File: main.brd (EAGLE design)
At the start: 100 x 50 mm, 116 parts, among them IC1 PM8834-SO08N, IC17 LD398533RM, IC18 LD1117S50TR, IC2 PM8834-SO08N, IC4 CP2102, J1 RJ11, Q1 IRF3205SPBF, Q11 BSS138, Q12 BSS138, Q13 BSS138, Q2 IRF3205SPBF, Q3 IRF3205SPBF, Q4 IRF3205SPBF, Q5 BSS138, Q6 BSS138, Q7 BSS138, Q8 BSS138, Q9 BSS138, T1 SS8050-G, T2 SS8050-G, U1 TMP275AIDR, U4 ESP-WROOM-32, X2 1751248, X4 1751277, X5 1751280

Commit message: Layout
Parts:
- removed C28, C29: 12pF, resistor:C0805
- removed C56, C62: 100nF, resistor:C0805
- removed C57: 10nF X7R, resistor:C0805
- removed C58, C61: 1uF_X5R, resistor:C0805
- removed C59, C60: 10uF, resistor:SMC_C
- removed D14: BAT60JFILM, diode:SOD323-W
- removed IC17: LD398533RM, st-microelectronics:SOT23-5L
- removed IC18: LD1117S50TR, v-reg:SOT223
- removed JP6: (no value), adafruit:1X03
- removed LED14: ROOD, led:CHIP-LED0805
- removed LED2: RGBLED5050, adafruit:RGBLED5050
- removed R44, R45: 10K, resistor:R0805
- removed R46: 10R, resistor:R0805
- removed R47: X, resistor:R0805
- removed R48: 1K, resistor:R0805
- removed U4: ESP-WROOM-32, esp32:ESP-WROOM-32
- removed X5: 1751280, con-phoenix-350:1751280
- added C17, C18, C20: 100n, resistor:C0805
- added C19, C7: 100nF, resistor:C0805
- added C21, C22: 1uF X7R, resistor:C0805
- added C9: (no value), resistor:SMC_A
- added IC3: CP2102, silabs:MLP28
- added IC5: PM8834-SO08N, PM8834:SO08N
- added JP2: (no value), adafruit:1X03
- added LED1: RGBLED5050, adafruit:RGBLED5050
- added U2: TMP275AIDR, TMP275AIDR:SOIC127P600X175-8N
- added X1: 1751248, con-phoenix-350:1751248
- C1: value 100n -> 10uF; device resistor:C0805 -> resistor:SMC_C
- C10: value 100n -> 1uF_X5R
- C11: value (none) -> 100nF; device resistor:SMC_A -> resistor:C0805
- C14, C15: value 100n -> 12pF
- C2: value 100nF -> 10uF; device resistor:C0805 -> resistor:SMC_C
- C3: value 100nF -> 1uF_X5R
- C5: value 1uF_X5R -> 10nF X7R
- C6: value 1uF X7R -> 1uF_X5R
- C8: value 1uF X7R -> 100nF
- D1, D2: value BAT54S -> BAT60JFILM; device diode:SOT23 -> diode:SOD323-W
- D5: value BAT60JFILM -> BAT54S; device diode:SOD323-W -> diode:SOT23
- IC1: value PM8834-SO08N -> LD1117S50TR; device PM8834:SO08N -> v-reg:SOT223
- IC2: value PM8834-SO08N -> LD398533RM; device PM8834:SO08N -> st-microelectronics:SOT23-5L
- IC4: value CP2102 -> PM8834-SO08N; device silabs:MLP28 -> PM8834:SO08N
- Q1: value IRF3205SPBF -> (none); device IRF3205SPBF:TRANS_IRF3205SPBF -> crystal:TC38H
- Q10: value (none) -> IRF3205SPBF; device crystal:TC38H -> IRF3205SPBF:TRANS_IRF3205SPBF
- Q11, Q12, Q13: value BSS138 -> IRF3205SPBF; device SparkFun:SOT23-3 -> IRF3205SPBF:TRANS_IRF3205SPBF
- Q2, Q3, Q4: value IRF3205SPBF -> BSS138; device IRF3205SPBF:TRANS_IRF3205SPBF -> SparkFun:SOT23-3
- R1: value 10K -> 22K1
- R10: value 10R -> 10K
- R11, R12, R29: value 10K -> 4K7
- R15, R16: value X -> 10K
- R17, R18, R38, R39: value 1K -> 10K
- R2: value 10R -> 47K5
- R21, R22: value 10K -> X
- R23, R24: value 10K -> 10R
- R25, R26, R34: value 10K -> 1K
- R3, R4: value 4K7 -> 1K
- R31, R32: value 0R -> 10K
- R33: value 2K -> 10K
- R35: value 22K1 -> 10K
- R36: value 47K5 -> 10K
- R5: value 4K7 -> 2K
- R7, R8: value 1K -> 0R
- S1: value (none) -> MOMENTARY-SWITCH-SPST-SMD-5.2-REDUNDANT; device switch-omron:B3F-10XX -> SparkFun-Switches:TACTILE_SWITCH_SMD_5.2MM
- U1: value TMP275AIDR -> ESP-WROOM-32; device TMP275AIDR:SOIC127P600X175-8N -> esp32:ESP-WROOM-32
- X2: value 1751248 -> 1751280; device con-phoenix-350:1751248 -> con-phoenix-350:1751280
- moved Q12 160.0 mm to (30.8, 6.03), turned to 270 degrees
- moved Q11 151.7 mm to (30.8, -6.03), turned to 270 degrees
- moved R40 147.9 mm to (9.84, 12.4), turned to 180 degrees
- moved R6 138.8 mm to (-6.99, -9.21), turned to 180 degrees
- moved C15 129.6 mm to (-19.7, 5.71), turned to 180 degrees
- moved D3 124.1 mm to (-40.3, 7.94), turned to 270 degrees
- moved Q9 104.5 mm to (-20.3, -7.30)
- moved Q4 103.6 mm to (-34.3, -62.5), turned to 90 degrees
- moved X2 94.1 mm to (-46.4, 4.76), turned to 270 degrees
- moved R29 93.1 mm to (9.84, 16.8), turned to 180 degrees
- moved R20 92.0 mm to (-37.1, -66.7), turned to 270 degrees
- moved Q3 91.6 mm to (-34.3, -58.4), turned to 90 degrees
- moved R19 91.2 mm to (-31.4, -66.7), turned to 90 degrees
- moved H1 90.0 mm to (45.0, 20.0)
- moved H2 90.0 mm to (45.0, -20.0)
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- renumbered C30 to C16, CN2 to CN1, S3 to S2, X4 to X3
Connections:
- removed net LED: U4.12
- removed net N$22: X5.1
- removed net N$28: Q13.3, R41.1
- removed net N$30: LED2.5, R40.1
- removed net N$33: D3.3, R46.2, R48.1
- removed net N$37: Q12.1
- removed net N$4: X5.4
- removed net N$40: Q11.1
- removed net N$41: Q9.1
- removed net N$99: LED14.A, R39.1
- new net LEDB: Q8.1, U1.12
- new net LEDG: Q7.1, U1.11
- new net LEDR: Q6.1, U1.10
- new net P1: Q9.3, R35.1, U1.16
- net +12V: now also C1.+, C21.1, C22.1, IC1.3, IC4.6, IC5.6, R38.2, R39.2, R42.2, R43.2, X1.1; no longer C59.+, C6.1, C8.1, IC1.6, IC18.3, IC2.6, R11.2, R12.2, R13.2, R14.2, X2.1
- net +3V3: now also C10.1, C11.1, C19.1, C6.1, C7.1, C8.1, C9.+, D4.2, IC2.5, IC3.6, IC3.7, LED1.1, LED1.2, LED1.3, Q2.1, Q3.1, Q4.1, R11.2, R12.2, R13.1, R15.1, R17.1, R19.1, R27.2, R28.2, R29.2, R35.2, U1.2, U2.8; no longer C11.+, C12.1, C13.1, C4.1, C5.1, C61.1, C62.1, D1.2, D2.2, IC17.5, IC4.6, IC4.7, LED2.1, LED2.2, LED2.3, Q6.1, Q7.1, Q8.1, R1.2, R23.1, R25.1, R27.1, R29.1, R33.2, R41.2, R6.2, R7.2, R8.2, R9.2, U1.8, U4.2
- net +5V: now also C3.1, C4.1, D1.C, D2.C, D5.2, IC2.1, IC2.3, JP1.1, R14.1, R33.2, X2.1, X2.4; no longer C56.1, C58.1, D14.C, D4.2, D5.C, IC17.1, IC17.3, JP6.1, R24.1, R37.2
- net BTN: now also C13.1, R4.1, S1.3, S1.4, U1.6; no longer C2.1, R8.1, S1.1, U4.6
- net CTS: now also IC3.23; no longer IC4.23
- net DCD: now also IC3.1; no longer IC4.1
- net DSR: now also IC3.27; no longer IC4.27
- net DTR: now also IC3.28, R9.1; no longer IC4.28, R42.1
- net EN: now also C12.1, R3.1, U1.3; no longer C3.1, R7.1, U4.3
- net GND: now also C1.-, C11.2, C17.2, C18.2, C19.2, C2.-, C20.2, C21.2, C22.2, C7.2, C9.-, D5.1, IC1.1, IC2.2, IC3.3, IC3.EXP, IC3.M, IC5.3, JP2.3, Q10.3, Q11.3, Q12.3, Q13.3, Q6.2, Q7.2, Q8.2, R2.1, R21.1, R22.1, R36.2, R37.2, R40.2, R41.2, R6.2, S1.1, S1.2, U1.1, U1.15, U1.38, U2.4, U2.5, U2.6, U2.7, X1.2, X2.3, X2.6; no longer C1.2, C11.-, C2.2, C28.2, C29.2, C56.2, C57.2, C58.2, C59.-, C60.-, C61.2, C62.2, D1.1, D2.1, IC1.3, IC17.2, IC18.1, IC2.3, IC4.EXP, IC4.M, JP6.3, LED14.C, Q1.3, Q11.2, Q12.2, Q13.2, Q2.3, Q3.3, Q4.3, R15.1, R16.1, R19.2, R20.2, R21.2, R22.2, R34.2, R36.1, R47.1, S1.3, U1.4, U1.5, U1.6, U1.7, U4.1, U4.15, U4.38, X2.2, X5.3, X5.6
- net HV: now also JP2.1, R16.1, R18.1, R20.1; no longer JP1.1, R26.1, R28.1, R30.1
- net HV1: now also JP1.2, Q2.3, R14.2; no longer JP6.2, Q5.3, R24.2
- net HV2: now also JP2.2, Q3.3, R16.2; no longer JP1.2, Q6.3, R26.2
- net HV3: now also Q4.3, R18.2; no longer Q7.3, R28.2
- net HV4: now also Q5.3, R20.2; no longer Q8.3, R30.2
- net I2C_SCL: now also R12.1, U1.36, U2.2; no longer R4.1, U1.2, U4.36
- net I2C_SDA: now also R11.1, U1.37, U2.1; no longer R3.1, U1.1, U4.37
- net INP1: now also C17.1, R25.2, R27.1, U1.13; no longer C10.1, R17.2, R9.1, U4.11
- net INP2: now also C18.1, R26.2, R28.1, U1.14; no longer C1.1, C15.1, R1.1, R18.2, R48.2, R6.1, U4.10
- net IO0: now also U1.25; no longer U4.25
- net LV0: now also Q2.2, R13.2; no longer Q5.2, R23.2
- net LV1: now also Q3.2, R15.2; no longer Q6.2, R25.2
- net LV2: now also Q4.2, R17.2; no longer Q7.2, R27.2
- net LV3: now also Q5.2, R19.2; no longer Q8.2, R29.2
- net N$1: now also Q6.3, R30.2; no longer Q9.3, R40.2
- net N$10: now also IC4.4, R38.1; no longer IC1.4, R11.1
- net N$102: now also C5.1, IC2.4; no longer C57.1, IC17.4
- net N$11: now also LED1.5, R31.1; no longer LED2.6, R44.1
- net N$12: now also IC4.7, Q11.1; no longer IC1.7, Q2.1
- net N$13: now also IC4.5, Q10.1; no longer IC1.5, Q1.1
- net N$14: now also Q11.2; no longer Q2.2
- net N$15: now also IC5.7, Q13.1; no longer IC2.7, Q4.1
- net N$16: now also IC5.5, Q12.1; no longer IC2.5, Q3.1
- net N$17: now also Q12.2; no longer Q3.2
- net N$18: now also Q13.2; no longer Q4.2
- net N$19: now also IC3.11, R6.1; no longer IC4.11, R34.1
- net N$2: now also R22.2, R24.1, X2.5; no longer R15.2, R2.1, X5.5
- net N$20: now also R21.2, R23.1, X2.2; no longer R10.1, R16.2, X5.2
- net N$2001: now also IC5.4, R43.1; no longer IC2.4, R14.1
- net N$21: now also IC3.9, R5.1; no longer IC4.9, R33.1
- net N$23: now also C2.+, D1.A, IC1.4; no longer C60.+, D14.A, IC18.4, R39.2
- net N$24: now also IC3.8, R1.2, R2.2; no longer IC4.8, R35.2, R36.2
- net N$25: now also IC3.5; no longer IC4.5
- net N$26: now also R33.1, R34.1; no longer R37.1, R38.1
- net N$27: now also C20.1, D5.3, Q9.1, R34.2; no longer C14.1, D4.3, Q13.1, R38.2
- net N$29: now also LED1.4, R32.1; no longer LED2.4, R45.1
- net N$2OO: now also IC5.1, R42.1; no longer IC2.1, R13.1
- net N$3: now also D3.3, R23.2, R25.1; no longer D2.3, R10.2, R17.1
- net N$31: now also Q7.3, R31.2; no longer Q11.3, R44.2
- net N$32: now also Q8.3, R32.2; no longer Q12.3, R45.2
- net N$38: now also C14.1, Q1.2, U1.8; no longer C28.1, Q10.2, U4.8
- net N$39: now also C15.1, Q1.1, U1.9; no longer C29.1, Q10.1, U4.9
- net N$42: now also R9.2; no longer R42.2
- net N$43: now also R10.2; no longer R43.2
- net N$5: now also LED1.6, R30.1; no longer R46.1, R47.2
- net N$6: now also IC3.4; no longer IC4.4
- net N$7: now also Q10.2; no longer Q1.2
- net N$8: now also D4.3, R24.2, R26.1; no longer D1.3, R18.1, R2.2
- net N$9: now also IC4.1, R39.1; no longer IC1.1, R12.1
- net PWM0: now also IC4.2, R36.1, U1.28; no longer IC1.2, R22.1, U4.28
- net PWM1: now also IC4.8, R37.1, U1.29; no longer IC1.8, R21.1, U4.29
- net PWM2: now also IC5.2, R40.1, U1.30; no longer IC2.2, R20.1, U4.30
- net PWM3: now also IC5.8, R41.1, U1.31; no longer IC2.8, R19.1, U4.31
- net RI: now also IC3.2; no longer IC4.2
- net RTS: now also IC3.24, R10.1; no longer IC4.24, R43.1
- net RXD: now also IC3.25, R8.1; no longer IC4.25, R32.1
- net RXD0: now also R7.2, U1.34; no longer R31.2, U4.34
- net TEMP_ALERT: now also R29.1, U1.33, U2.3; no longer R5.1, U1.3, U4.33
- net TXD: now also IC3.26, R7.1; no longer IC4.26, R31.1
- net TXD0: now also R8.2, U1.35; no longer R32.2, U4.35
- net VBUS: now also D2.A, R1.1; no longer D5.A, R35.1
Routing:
- net +3V3: track 104.0 -> 196.1 mm, vias 9 -> 15
- net +5V: track 5.22 -> 48.6 mm
- net LEDB: track 0.00 -> 40.3 mm, vias 0 -> 2
- net LEDG: track 0.00 -> 35.9 mm, vias 0 -> 2
- net LEDR: track 0.00 -> 33.2 mm, vias 0 -> 2
- net INP1: track 6.01 -> 34.3 mm, vias 0 -> 2
- net INP2: track 6.68 -> 33.9 mm, vias 0 -> 2
- net BTN: track 2.23 -> 26.7 mm, vias 0 -> 4
- net P1: track 0.00 -> 17.0 mm
- net N$38: track 0.00 -> 12.8 mm
- net N$29: track 0.00 -> 11.5 mm, vias 0 -> 2
- net VBUS: track 4.78 -> 15.1 mm, vias 0 -> 2
- net N$11: track 0.00 -> 8.93 mm, vias 0 -> 2
- net N$23: track 24.0 -> 31.9 mm, vias 1 -> 2
- net N$32: track 0.00 -> 6.97 mm
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
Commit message: All routed
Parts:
- removed JP3, JP4: (no value), adafruit:1X03
- removed Q4, Q5: BSS138, SparkFun:SOT23-3
- removed R17, R18, R19, R20: 10K, resistor:R0805
- moved Q2 44.8 mm to (-36.8, -9.53)
- moved Q3 44.8 mm to (-36.8, -13.7)
- moved R13 44.8 mm to (-34.0, -9.53)
- moved R14 44.8 mm to (-39.7, -9.53)
- moved R15 44.8 mm to (-34.0, -13.7)
- moved R16 44.8 mm to (-39.7, -13.7)
- moved JP2 44.5 mm to (-45.1, -12.4)
- moved JP1 44.5 mm to (-45.1, -9.84)
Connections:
- removed net HV: JP2.1, JP3.1, JP4.1, R16.1, R18.1, R20.1
- removed net HV3: JP3.2, Q4.3, R18.2
- removed net HV4: JP4.2, Q5.3, R20.2
- removed net LV2: Q4.2, R17.2
- removed net LV3: Q5.2, R19.2
- net +3V3: no longer Q4.1, Q5.1, R17.1, R19.1
- net +5V: now also JP2.1, R16.1
- net GND: no longer JP3.3, JP4.3
- net LV0: now also U1.23
- net LV1: now also U1.27
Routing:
- net LV1: track 1.86 -> 54.2 mm, vias 0 -> 2
- net LV0: track 1.86 -> 45.6 mm, vias 0 -> 2
- net +5V: track 48.6 -> 86.5 mm, vias 0 -> 1
- net HV2: track 2.15 -> 8.47 mm, vias 0 -> 1
- net HV1: track 2.15 -> 8.34 mm, vias 0 -> 1
- net +3V3: track 196.1 -> 191.7 mm, vias 15 -> 13
- net HV4: track 2.15 -> 0.00 mm
- net HV3: track 2.15 -> 0.00 mm
- net LV3: track 1.86 -> 0.00 mm
- net LV2: track 1.86 -> 0.00 mm
- net P1: track 17.0 -> 17.5 mm
- net GND: vias 39 -> 59

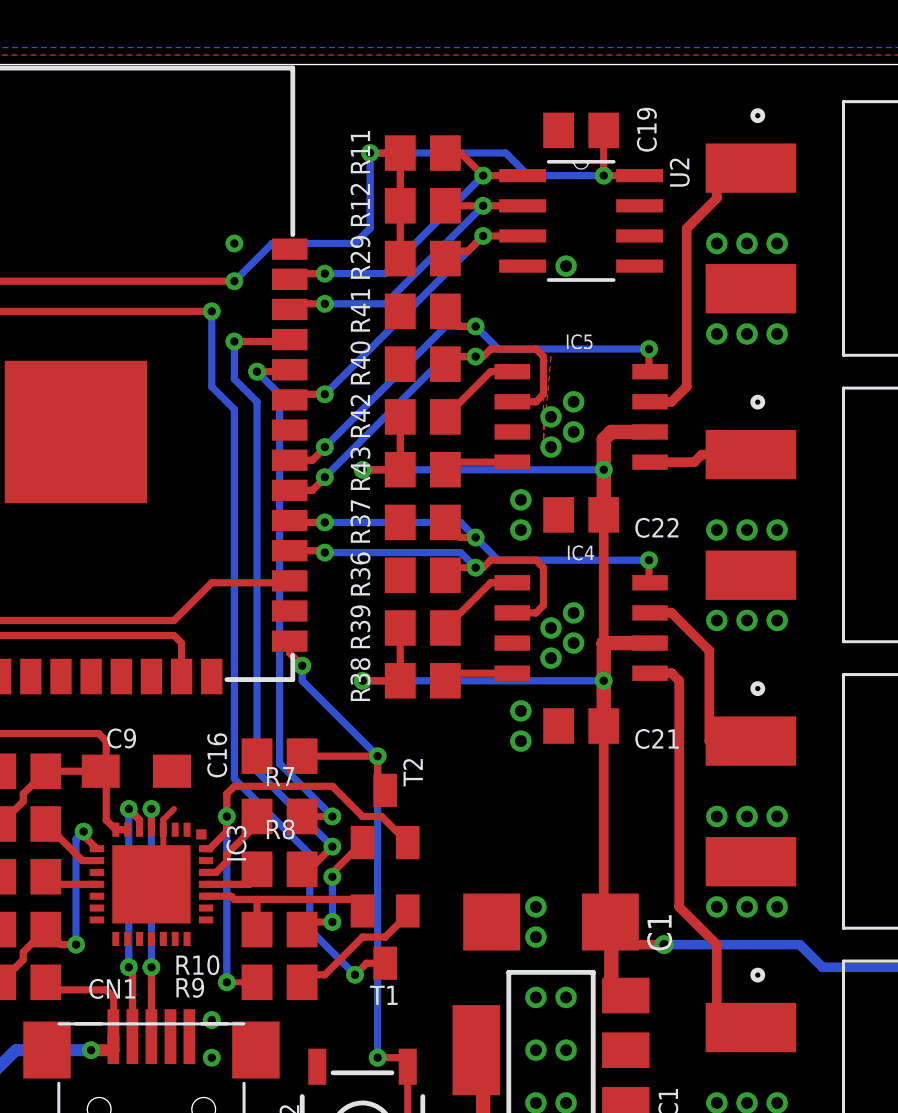
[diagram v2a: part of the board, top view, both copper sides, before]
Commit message: Added light sensor
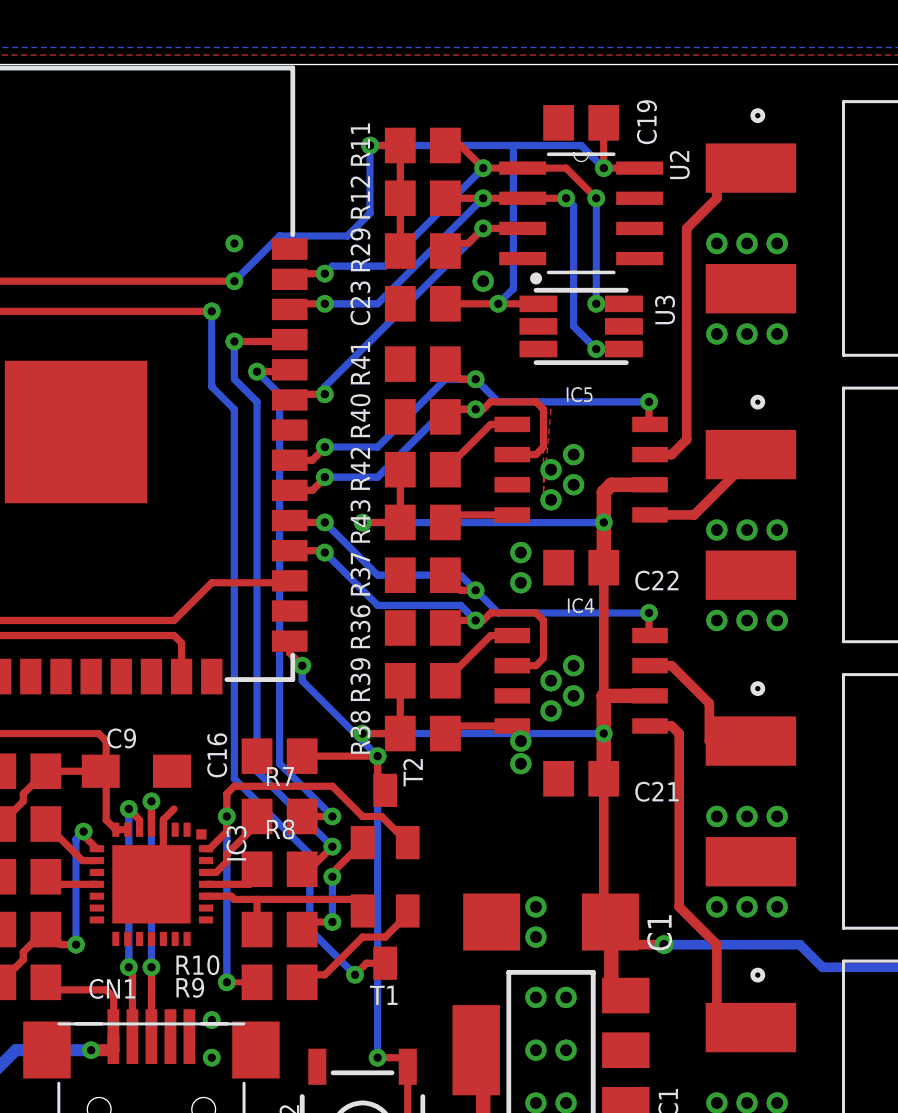
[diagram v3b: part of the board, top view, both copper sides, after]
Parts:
- added C23: 100nF, resistor:C0805
- added U3: TSL2561T, SparkFun-Sensors:TMB-6
- moved C21 2.22 mm to (16.5, -5.08)
- moved IC4 2.22 mm to (16.5, -0.95)
- moved IC5 2.22 mm to (16.5, 7.94)
- moved R36 2.22 mm to (9.84, 1.27)
- moved R39 2.22 mm to (9.84, -0.95)
- moved R40 2.22 mm to (9.84, 10.2)
- moved R41 2.22 mm to (9.84, 12.4)
- moved R42 2.22 mm to (9.84, 7.94)
- moved R43 2.22 mm to (9.84, 5.71)
- moved C22 2.22 mm to (16.5, 3.81)
- moved R37 2.22 mm to (9.84, 3.49)
- moved R38 2.22 mm to (9.84, -3.17)
- moved U2 0.32 mm to (16.5, 18.7)
- moved C19 0.32 mm to (16.5, 22.5)
- moved R11 0.32 mm to (9.84, 21.6)
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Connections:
- net +3V3: now also C23.1, U3.1
- net GND: now also C23.2, U3.2, U3.3
- net I2C_SCL: now also U3.4
- net I2C_SDA: now also U3.6
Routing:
- net +3V3: track 191.7 -> 202.5 mm, vias 13 -> 14
- net I2C_SCL: track 13.2 -> 23.2 mm, vias 2 -> 4
- net I2C_SDA: track 13.6 -> 23.0 mm, vias 2 -> 4
- net N$12: track 8.72 -> 6.49 mm
- net N$15: track 12.8 -> 15.0 mm
- net N$13: track 17.7 -> 15.5 mm
- net +12V: track 85.4 -> 83.1 mm
- net N$16: track 4.38 -> 5.39 mm
- net PWM2: track 17.7 -> 16.8 mm
- net PWM3: track 20.4 -> 19.5 mm
- net PWM1: track 18.4 -> 19.3 mm
- net PWM0: track 16.0 -> 16.9 mm
- net N$6: track 10.5 -> 11.1 mm

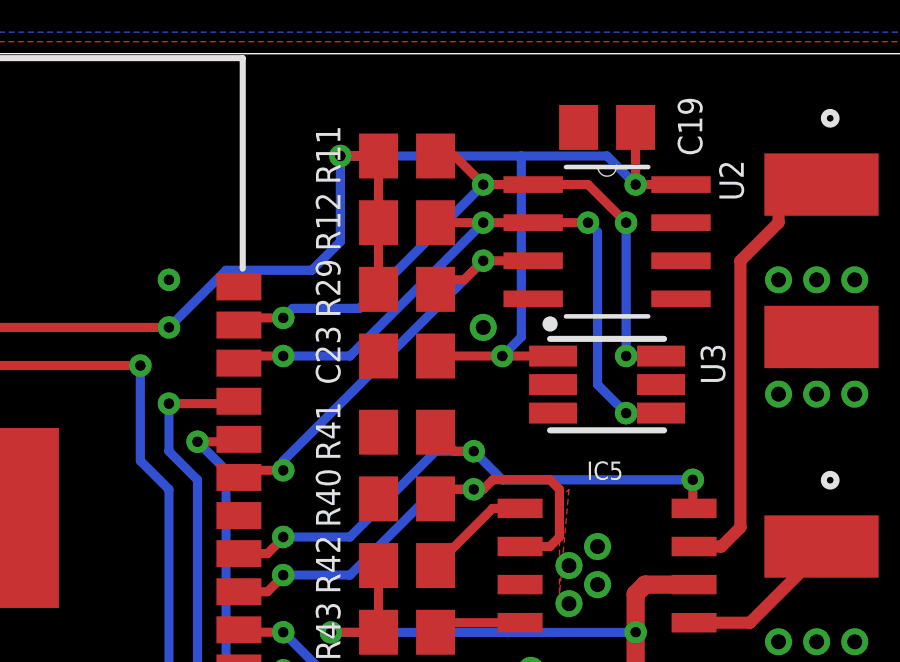
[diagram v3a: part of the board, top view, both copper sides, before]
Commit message: Removed temp alert signal
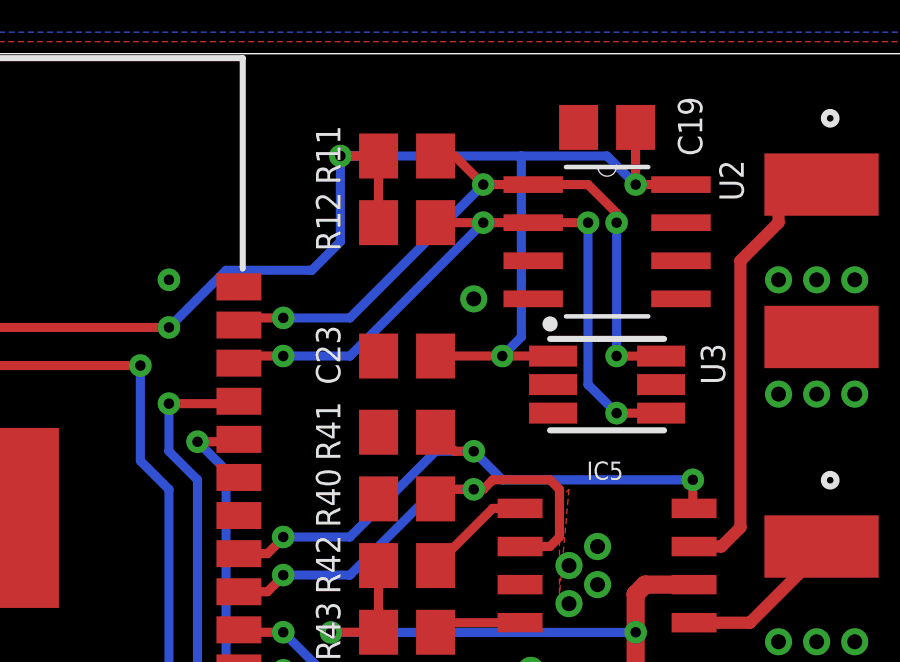
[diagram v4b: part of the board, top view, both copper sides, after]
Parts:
- removed R29: 4K7, resistor:R0805
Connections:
- removed net TEMP_ALERT: R29.1, U1.33, U2.3
- net +3V3: no longer R29.2
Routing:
- net TEMP_ALERT: track 15.0 -> 0.00 mm, vias 2 -> 0
- net +3V3: track 202.5 -> 200.3 mm
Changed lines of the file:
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@@
 <attribute name="VALUE" x="10.4775" y="21.9075" size="1.27" layer="27" rot="R180"/>
-</element>
-<element name="R29" library="resistor" library_urn="urn:adsk.eagle:library:348" package="R0805" package3d_urn="urn:adsk.eagle:package:23553/2" value="4K7" x="9.8425" y="17.145" smashed="yes" rot="R180">
-<attribute name="NAME" x="7.62" y="16.1925" size="0.8128" layer="25" rot="R90"/>
-<attribute name="VALUE" x="10.4775" y="19.685" size="1.27" layer="27" rot="R180"/>
 </element>
 <element name="C8" library="resistor" library_urn="urn:adsk.eagle:library:348" package="C0805" package3d_urn="urn:adsk.eagle:package:23617/2" value="100nF" x="-17.145" y="17.145" smashed="yes" rot="R90">
@@
 <via x="14.605" y="-11.7475" extent="1-16" drill="0.5"/>
 <via x="14.605" y="-10.4775" extent="1-16" drill="0.5"/>
-<via x="12.3825" y="15.875" extent="1-16" drill="0.5"/>
+<via x="12.065" y="16.8275" extent="1-16" drill="0.5"/>
 <via x="-20.6375" y="7.3025" extent="1-16" drill="0.35"/>
 <via x="-24.765" y="7.3025" extent="1-16" drill="0.35"/>
@@
 <contactref element="R11" pad="2"/>
 <contactref element="R12" pad="2"/>
-<contactref element="R29" pad="2"/>
 <contactref element="R3" pad="2"/>
 <contactref element="U1" pad="2"/>
@@
 <wire x1="8.8925" y1="19.3675" x2="8.8925" y2="21.59" width="0.3048" layer="1"/>
 <wire x1="7.62" y1="21.59" x2="8.8925" y2="21.59" width="0.3048" layer="1"/>
-<wire x1="8.8925" y1="17.145" x2="8.8925" y2="19.3675" width="0.3048" layer="1"/>
 <contactref element="R13" pad="1"/>
 <contactref element="Q2" pad="1"/>
@@
 <wire x1="14.0462" y1="20.6375" x2="12.3825" y2="20.6375" width="0.3048" layer="1"/>
 <via x="12.3825" y="20.6375" extent="1-16" drill="0.35"/>
-<wire x1="12.3825" y1="20.6375" x2="8.255" y2="16.51" width="0.3048" layer="16"/>
-<wire x1="8.255" y1="16.51" x2="6.0325" y2="16.51" width="0.3048" layer="16"/>
-<wire x1="5.715" y1="16.1925" x2="6.0325" y2="16.51" width="0.3048" layer="16"/>
+<wire x1="12.3825" y1="20.6375" x2="7.9375" y2="16.1925" width="0.3048" layer="16"/>
+<wire x1="7.9375" y1="16.1925" x2="5.715" y2="16.1925" width="0.3048" layer="16"/>
 <contactref element="R11" pad="1"/>
 <contactref element="U1" pad="37"/>
@@
 <wire x1="11.43" y1="21.59" x2="12.3825" y2="20.6375" width="0.3048" layer="1"/>
 <contactref element="U3" pad="6"/>
-<wire x1="18.31" y1="14.92" x2="17.1475" y2="14.92" width="0.3048" layer="1"/>
-<wire x1="17.1475" y1="14.92" x2="17.145" y2="14.9225" width="0.3048" layer="1"/>
-<via x="17.145" y="14.9225" extent="1-16" drill="0.35"/>
-<wire x1="17.145" y1="14.9225" x2="17.145" y2="19.3675" width="0.3048" layer="16"/>
-<via x="17.145" y="19.3675" extent="1-16" drill="0.35"/>
-<wire x1="17.145" y1="19.3675" x2="15.875" y2="20.6375" width="0.3048" layer="1"/>
+<wire x1="18.31" y1="14.92" x2="16.83" y2="14.92" width="0.3048" layer="1"/>
+<wire x1="16.83" y1="14.92" x2="16.8275" y2="14.9225" width="0.3048" layer="1"/>
+<via x="16.8275" y="14.9225" extent="1-16" drill="0.35"/>
+<wire x1="16.8275" y1="19.3675" x2="16.8275" y2="14.9225" width="0.3048" layer="16"/>
+<via x="16.8275" y="19.3675" extent="1-16" drill="0.35"/>
+<wire x1="16.8275" y1="19.3675" x2="16.8275" y2="19.685" width="0.3048" layer="1"/>
+<wire x1="16.8275" y1="19.685" x2="15.875" y2="20.6375" width="0.3048" layer="1"/>
 <wire x1="15.875" y1="20.6375" x2="14.0462" y2="20.6375" width="0.3048" layer="1"/>
 </signal>
@@
 <wire x1="14.0462" y1="19.3675" x2="15.875" y2="19.3675" width="0.3048" layer="1"/>
 <via x="15.875" y="19.3675" extent="1-16" drill="0.35"/>
-<wire x1="16.1925" y1="13.97" x2="17.145" y2="13.0175" width="0.3048" layer="16"/>
-<wire x1="15.875" y1="19.3675" x2="16.1925" y2="19.05" width="0.3048" layer="16"/>
-<wire x1="16.1925" y1="19.05" x2="16.1925" y2="13.97" width="0.3048" layer="16"/>
-<via x="17.145" y="13.0175" extent="1-16" drill="0.35"/>
-<wire x1="17.145" y1="13.0175" x2="18.3075" y2="13.0175" width="0.3048" layer="1"/>
+<wire x1="15.875" y1="13.97" x2="16.8275" y2="13.0175" width="0.3048" layer="16"/>
+<wire x1="15.875" y1="19.3675" x2="15.875" y2="13.97" width="0.3048" layer="16"/>
+<via x="16.8275" y="13.0175" extent="1-16" drill="0.35"/>
+<wire x1="16.8275" y1="13.0175" x2="18.3075" y2="13.0175" width="0.3048" layer="1"/>
 <wire x1="18.3075" y1="13.0175" x2="18.31" y2="13.02" width="0.3048" layer="1"/>
 </signal>
-<signal name="TEMP_ALERT">
-<contactref element="U2" pad="3"/>
-<contactref element="R29" pad="1"/>
-<contactref element="U1" pad="33"/>
-<wire x1="5.715" y1="11.1125" x2="4.475" y2="11.1125" width="0.3048" layer="1"/>
-<wire x1="4.2375" y1="10.875" x2="4.475" y2="11.1125" width="0.3048" layer="1"/>
-<via x="5.715" y="11.1125" extent="1-16" drill="0.35"/>
-<via x="12.3825" y="18.0975" extent="1-16" drill="0.35"/>
-<wire x1="14.0462" y1="18.0975" x2="12.3825" y2="18.0975" width="0.3048" layer="1"/>
-<wire x1="11.7475" y1="17.4625" x2="11.11" y2="17.4625" width="0.3048" layer="1"/>
-<wire x1="10.7925" y1="17.145" x2="11.11" y2="17.4625" width="0.3048" layer="1"/>
-<wire x1="11.7475" y1="17.4625" x2="12.3825" y2="18.0975" width="0.3048" layer="1"/>
-<wire x1="12.3825" y1="18.0975" x2="5.715" y2="11.43" width="0.3048" layer="16"/>
-<wire x1="5.715" y1="11.43" x2="5.715" y2="11.1125" width="0.3048" layer="16"/>
-</signal>
 <signal name="TXD0">
